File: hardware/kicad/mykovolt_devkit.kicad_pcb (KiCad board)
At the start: 4 copper layers, 30 x 20 mm, 57 parts, among them J1 SWD_2x5, J2 Pressling, J3 Aux_I2C, J4 Sensor_In, Q1 SI1308EDL, U1 STM32L011F4Px, U2 BQ25570, U3 ST25DV04K, U4 MB85RC16, U5 PCF8523T, U6 FDC1004, X1 32.768kHz

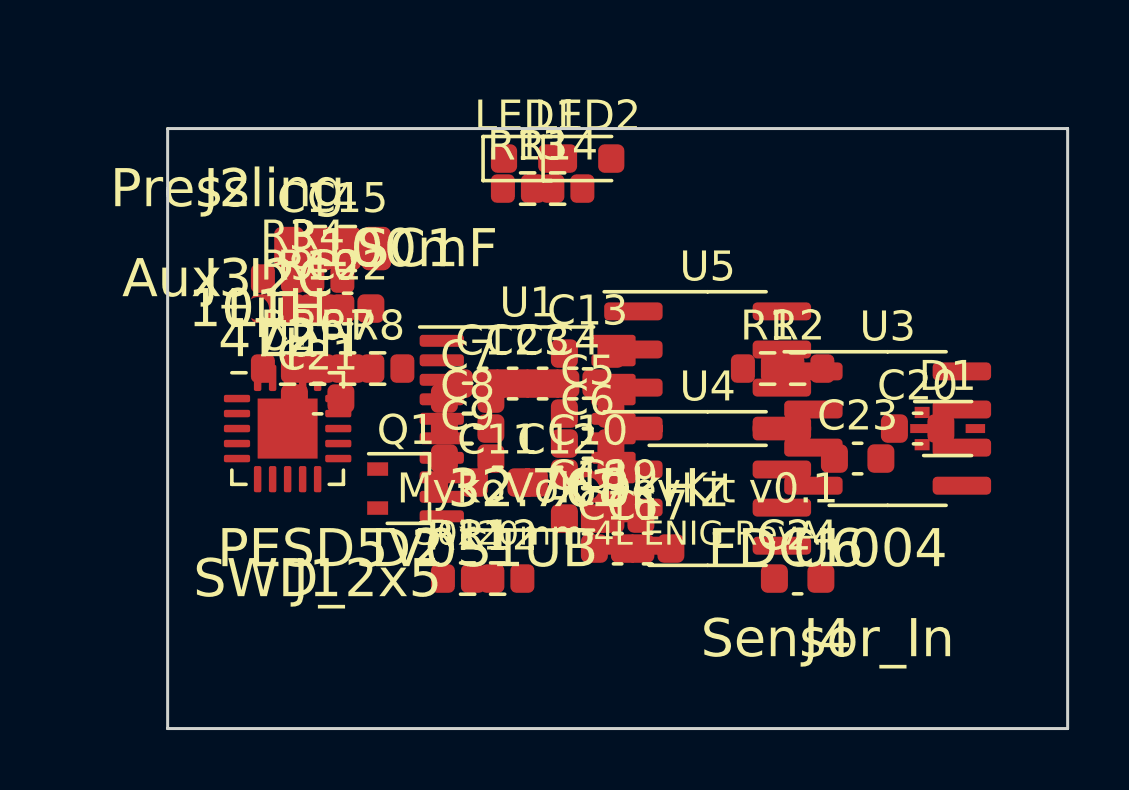
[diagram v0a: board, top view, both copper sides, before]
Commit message: feat: fix all 57 PCB footprints, add copper zones, create firmware structure
PCB improvements:
- Fixed all 10 failing footprint names for KiCad 6 library compatibility
  (Package_SON, Inductor_SMD, Crystal, PinHeader, JST, THT cap, SOD)
- All 57 footprints now load successfully with pcbnew (0 warnings)
- Added GND copper pour on In1.Cu (inner layer 1)
- Added 3.3V copper pour on In2.Cu (inner layer 2)
- Pad net assignments from netlist (pads connected to correct nets)
- PCB size: 212662 bytes, 57 footprints, 2 copper zones

Firmware structure (STM32L011F4, bare-metal):
- firmware/README.md — architecture, pin map, power tree, I2C bus map
- Core/Inc/mykovolt.h — board definitions, pin mappings, I2C addresses
- Core/Inc/i2c_driver.h + .c — register-level I2C master (100kHz)
- Core/Inc/fdc1004.h — FDC1004 capacitance sensor driver header
- Core/Inc/st25dv04k.h — ST25DV04K NFC tag driver header
- Core/Src/main.c — app states: SLEEP → ACTIVE → NFC_ACCESS cycle
- CMakeLists.txt + cmake/arm-gcc-toolchain.cmake — build system
- Power-gated sleep with RTC wake, NFC mailbox data exchange

Generator: 57 components, 35 nets, 185 connections, 0 warnings, 0 errors
Verification: 22/22 checks pass
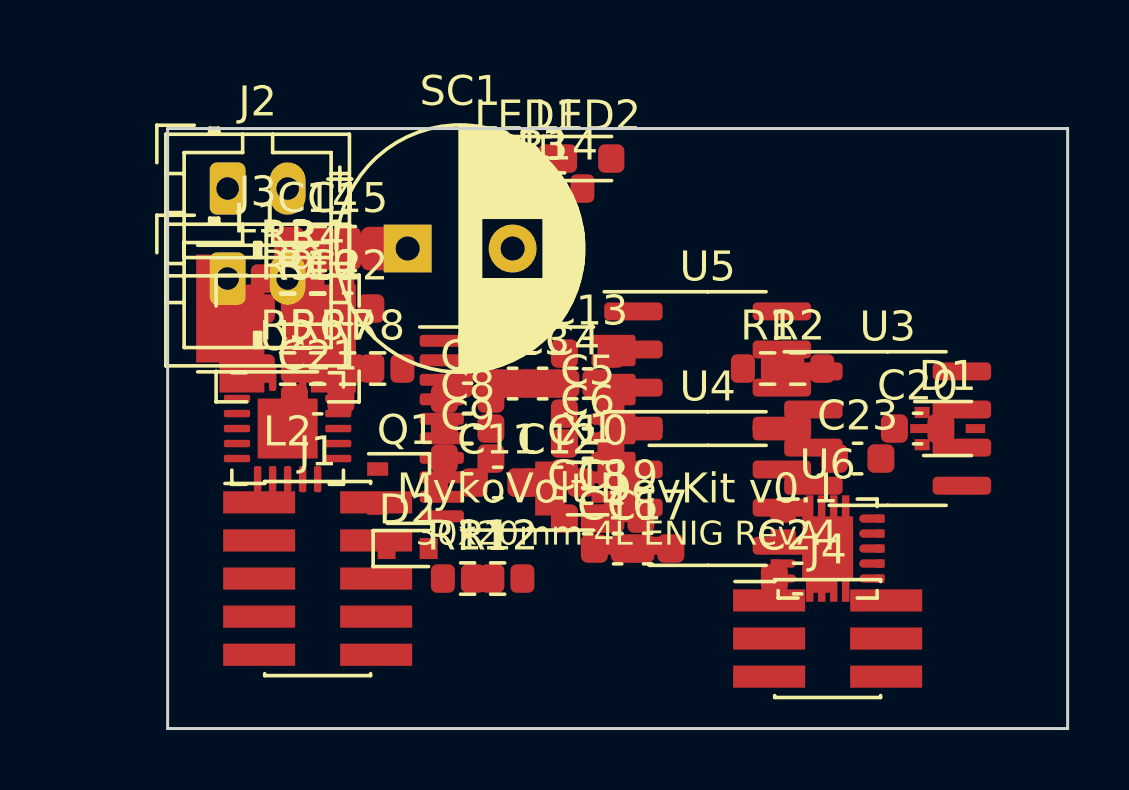
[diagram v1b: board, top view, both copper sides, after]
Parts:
- D2: footprint (none) -> D_SOD-523
- J1: footprint (none) -> PinHeader_2x05_P1.27mm_Vertical_SMD
- J2, J3: footprint (none) -> JST_PH_B2B-PH-K_1x02_P2.00mm_Vertical
- J4: footprint (none) -> PinHeader_2x03_P1.27mm_Vertical_SMD
- L1: footprint (none) -> L_Vishay_IFSC-1515AH_4x4x1.8mm
- L2: footprint (none) -> L_Bourns-SRN4018
- SC1: footprint (none) -> CP_Radial_D8.0mm_P3.50mm
- U6: footprint (none) -> Texas_S-PWSON-N10
- X1: footprint (none) -> Crystal_SMD_3215-2Pin_3.2x1.5mm
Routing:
- added copper zone on In2.Cu, net 3.3V
- added copper zone on In1.Cu, net GND
